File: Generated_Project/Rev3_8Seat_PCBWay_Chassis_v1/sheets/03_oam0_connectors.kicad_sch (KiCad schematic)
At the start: 0 parts

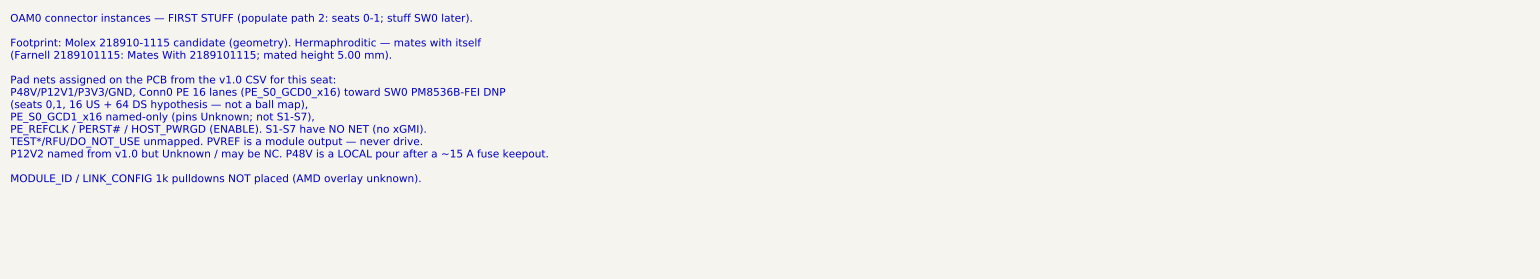
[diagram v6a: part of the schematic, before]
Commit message: Retarget Rev3 first article to seats 0-1 GCD0 x16 (2-module path).
Same 8-seat PCB. Without overlay, 2x MI250X means two modules can sit
and at most GCD0 on each can be named toward the host keepout (2 GCDs),
not 2x full-width (4 GCDs). Conn0 OCP PCIE_* is the only legal host PE.
No CEM/MCIO MPN. Do not energize P48V.

Co-authored-by: zivzancoeli-commits <zivzancoeli-commits@users.noreply.github.com>
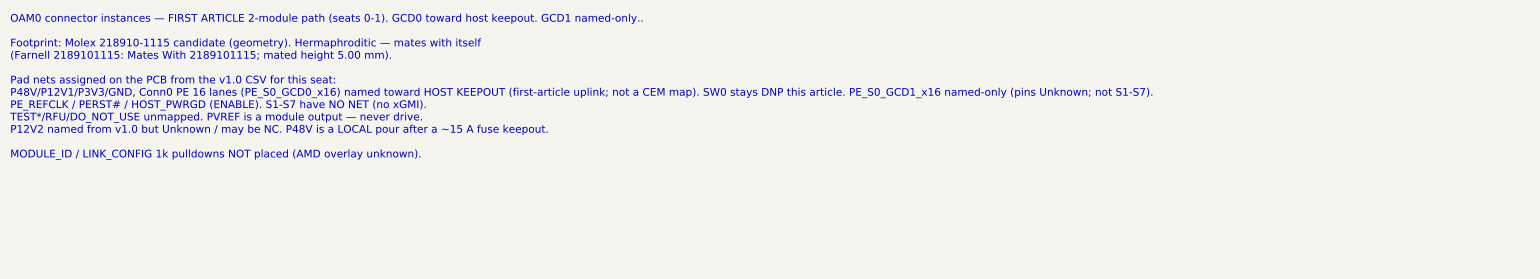
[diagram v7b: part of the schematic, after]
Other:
- note added: "OAM0 connector instances — FIRST ARTICLE 2-module path (seats 0-1). GCD0 toward host keepout. GCD1 named-only.. Footprint: Molex 218910-1115 candidate (geometry). Hermaphroditic — mates with itself (Farnell 2189101115: Mates With 2189101115; mated height 5.00 mm). Pad nets assigned on the PCB from the v1.0 CSV for this seat: P48V/P12V1/P3V3/GND, Conn0 PE 16 lanes (PE_S0_GCD0_x16) named toward HOS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"
- note removed: "OAM0 connector instances — FIRST STUFF (populate path 2: seats 0-1; stuff SW0 later). Footprint: Molex 218910-1115 candidate (geometry). Hermaphroditic — mates with itself (Farnell 2189101115: Mates With 2189101115; mated height 5.00 mm). Pad nets assigned on the PCB from the v1.0 CSV for this seat: P48V/P12V1/P3V3/GND, Conn0 PE 16 lanes (PE_S0_GCD0_x16) toward SW0 PM8536B-FEI DNP (seats 0,1, 16 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"
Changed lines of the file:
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@@
         (comment 4 "r2.0 UNUSABLE. P3V3=Conn0 C1/C2. 12L 2.0mm stuffed-switch TARGET. 4x PM8536 DNP. Star-fed P48V.")
 	)
-	(text "OAM0 connector instances — FIRST STUFF (populate path 2: seats 0-1; stuff SW0 later).\n\nFootprint: Molex 218910-1115 candidate (geometry). Hermaphroditic — mates with itself\n(Farnell 2189101115: Mates With 2189101115; mated height 5.00 mm).\n\nPad nets assigned on the PCB from the v1.0 CSV for this seat:\nP48V/P12V1/P3V3/GND, Conn0 PE 16 lanes (PE_S0_GCD0_x16) toward SW0 PM8536B-FEI DNP\n(seats 0,1, 16 US + 64 DS hypothesis — not a ball map),\nPE_S0_GCD1_x16 named-only (pins Unknown; not S1-S7),\nPE_REFCLK / PERST# / HOST_PWRGD (ENABLE). S1-S7 have NO NET (no xGMI).\nTEST*/RFU/DO_NOT_USE unmapped. PVREF is a module output — never drive.\nP12V2 named from v1.0 but Unknown / may be NC. P48V is a LOCAL pour after a ~15 A fuse keepout.\n\nMODULE_ID / LINK_CONFIG 1k pulldowns NOT placed (AMD overlay unknown).\n"
+	(text "OAM0 connector instances — FIRST ARTICLE 2-module path (seats 0-1). GCD0 toward host keepout. GCD1 named-only..\n\nFootprint: Molex 218910-1115 candidate (geometry). Hermaphroditic — mates with itself\n(Farnell 2189101115: Mates With 2189101115; mated height 5.00 mm).\n\nPad nets assigned on the PCB from the v1.0 CSV for this seat:\nP48V/P12V1/P3V3/GND, Conn0 PE 16 lanes (PE_S0_GCD0_x16) named toward HOST KEEPOUT (first-article uplink; not a CEM map). SW0 stays DNP this article. PE_S0_GCD1_x16 named-only (pins Unknown; not S1-S7).\nPE_REFCLK / PERST# / HOST_PWRGD (ENABLE). S1-S7 have NO NET (no xGMI).\nTEST*/RFU/DO_NOT_USE unmapped. PVREF is a module output — never drive.\nP12V2 named from v1.0 but Unknown / may be NC. P48V is a LOCAL pour after a ~15 A fuse keepout.\n\nMODULE_ID / LINK_CONFIG 1k pulldowns NOT placed (AMD overlay unknown).\n"
 		(exclude_from_sim no)
 		(at 20.32 20.32 0)
